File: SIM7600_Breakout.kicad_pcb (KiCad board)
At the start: 4 copper layers, 40 x 80 mm, 67 parts, among them J1 SIM8060-6-0-14-00-A, J2 2W Header, J3 MJ-3502N, J4 30W Header, J5 USB_B_Micro, J6 U.FL-R-SMT-1(01), J7 U.FL-R-SMT-1(01), J8 U.FL-R-SMT-1(01), Q1 MMBT3904L_RFG, U1 NVT2008PW_118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

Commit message: Added USB C to schematic & half assed putting it on the PCB
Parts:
- added R24: 5K1, Resistor_SMD:R_0201_0603Metric_Pad0.64x0.40mm_HandSolder, F.Cu at (141.6, 67.8)
- added R5: 5K1, Resistor_SMD:R_0201_0603Metric_Pad0.64x0.40mm_HandSolder, F.Cu at (129.8, 67.8)
- J5: value USB_B_Micro -> 2137160001; footprint sim7600_breakout:USB3100-30-A -> sim7600_breakout:2137160001-USB-C
- moved J5 3.58 mm to (138.7, 70.5)
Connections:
- D3 pad C: /D- -> /D+
- D4 pad C: /D+ -> /D-
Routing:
- net /PWRKEY: track 39.0 -> 15.6 mm, vias 2 -> 0
- net unconnected-(J5-Pad6): track 11.8 -> 0.00 mm
- net /D-: track 21.3 -> 19.9 mm
- net GND: track 96.2 -> 95.0 mm, vias 83 -> 81
- net /D+: track 21.2 -> 20.1 mm

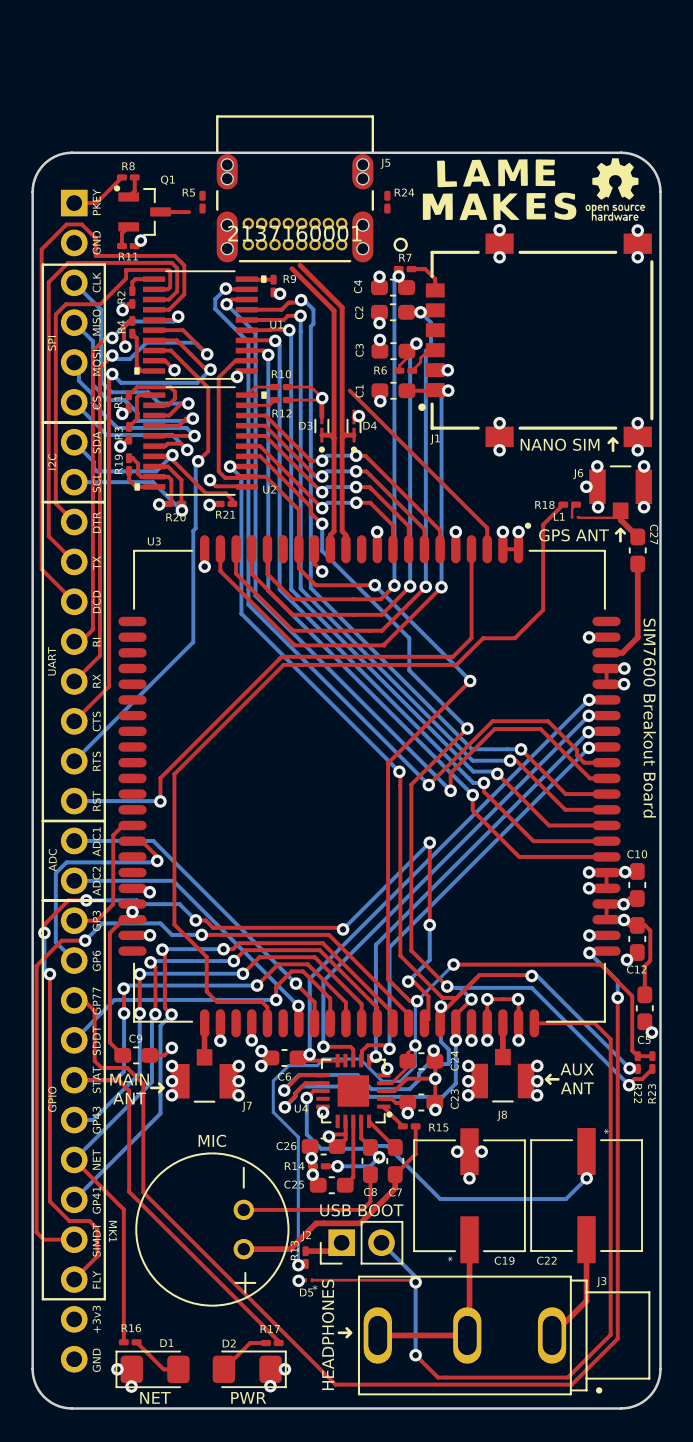
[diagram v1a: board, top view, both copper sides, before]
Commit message: Cleaning up USB-C addition
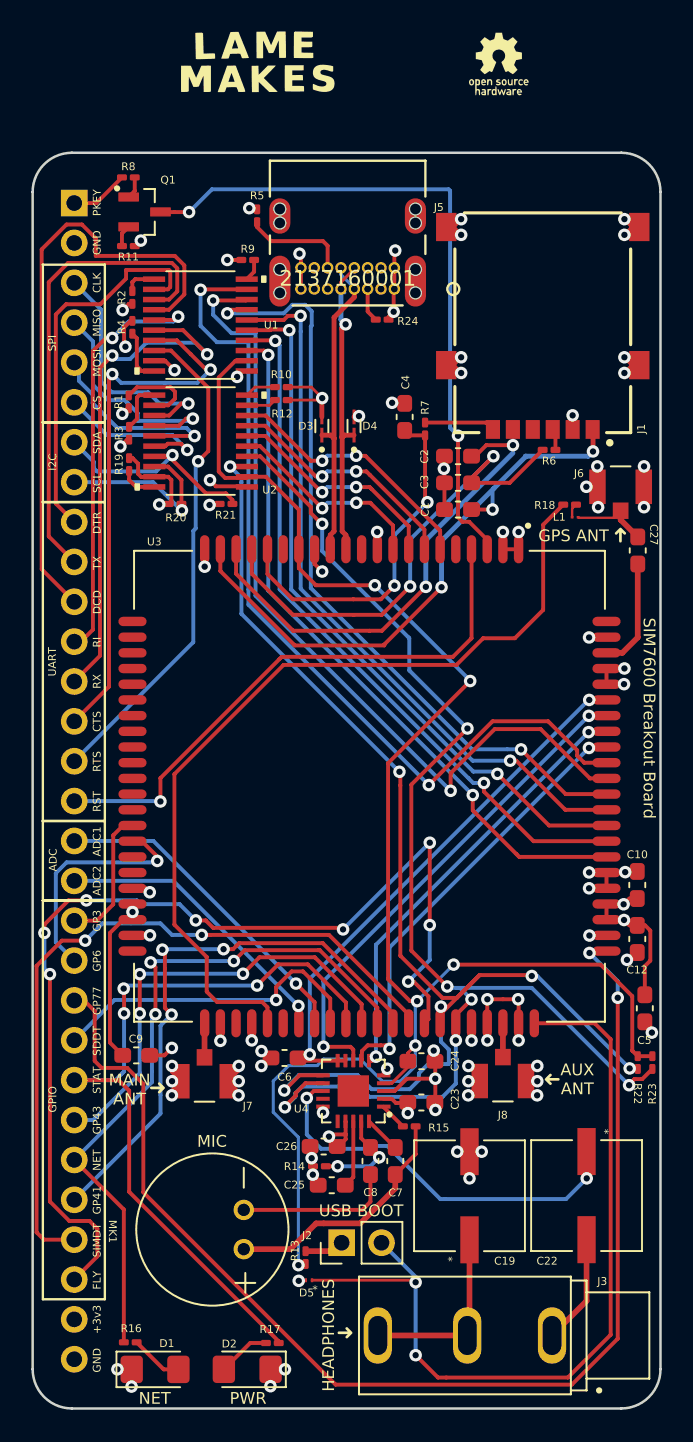
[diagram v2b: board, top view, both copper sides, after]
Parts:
- removed the G*** at (156.0, 83.3)
- moved G*** 17.4 mm to (133.3, 58.9)
- moved G*** 10.9 mm to (148.7, 59.0)
- moved R6 10.4 mm to (151.9, 83.6)
- moved R7 10.3 mm to (144.0, 82.3), turned to -90 degrees
- moved C2 10.1 mm to (146.1, 84.0)
- moved C3 9.35 mm to (146.1, 85.7)
- moved C1 8.61 mm to (146.1, 87.4)
- moved C4 8.27 mm to (142.7, 81.5), turned to 90 degrees
- moved R24 7.49 mm to (141.3, 75.3), turned to 180 degrees
- moved J5 4.38 mm to (142.0, 73.3)
- moved R5 3.58 mm to (133.3, 68.7), turned to -90 degrees
- moved R9 2.34 mm to (132.7, 71.5), turned to 0 degrees
- moved J1 1.12 mm to (151.5, 75.5), turned to 180 degrees
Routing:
- net /PWRKEY: track 15.6 -> 43.2 mm, vias 0 -> 2
- net /SIM_DATA: track 31.9 -> 22.6 mm
- net GND: track 95.0 -> 104.2 mm, vias 81 -> 82
- net Net-(J5-CC2): track 0.00 -> 6.71 mm
- net /SIM_CLK: track 36.1 -> 30.6 mm
- net /SIM_VCC: track 34.4 -> 38.1 mm, vias 2 -> 3
- net /UART_DTR: track 53.2 -> 56.0 mm
- net /UART_TX: track 51.8 -> 54.1 mm
- net /UART_DCD: track 46.8 -> 49.0 mm
- net Net-(J5-CC1): track 0.00 -> 2.16 mm
- net Net-(J1-IO): track 2.50 -> 4.51 mm
- net Net-(J1-RST): track 2.17 -> 1.37 mm
- net /D+: track 20.1 -> 19.8 mm, vias 0 -> 1
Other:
- board text removed: "NANO SIM"

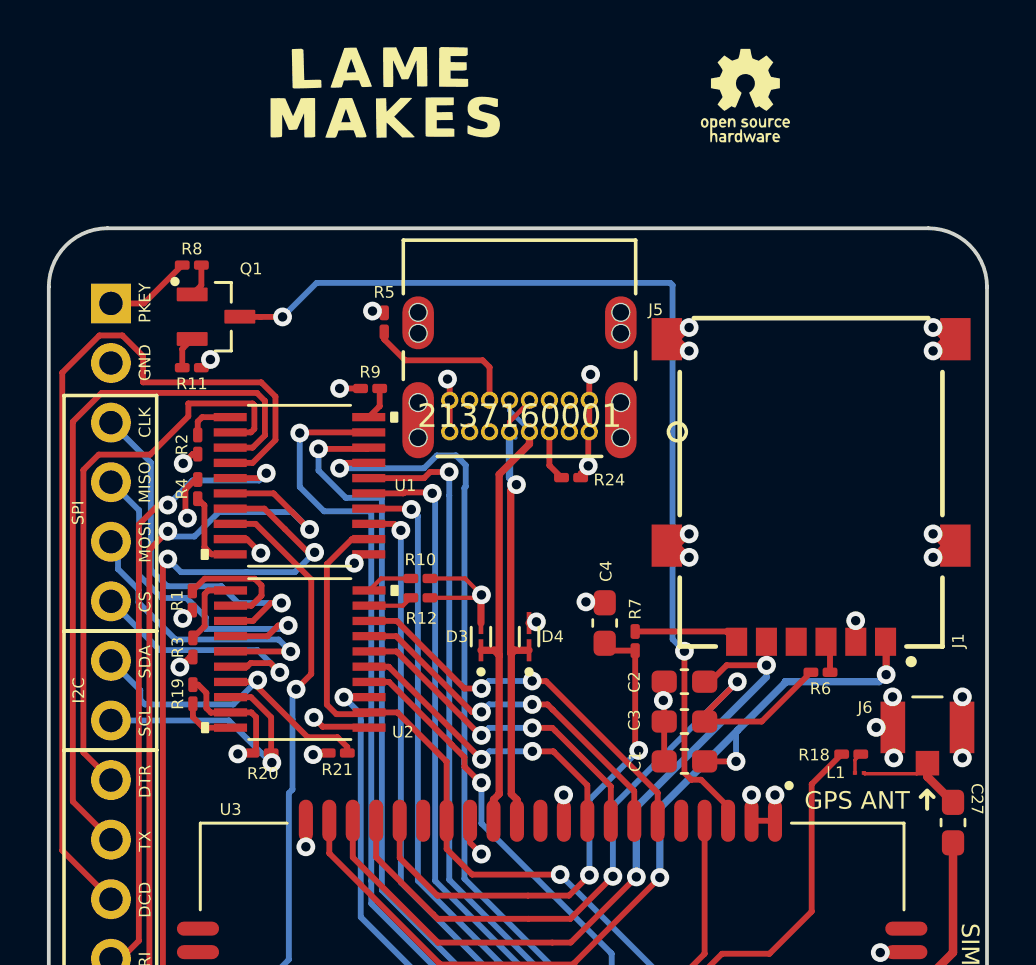
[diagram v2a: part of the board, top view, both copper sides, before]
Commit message: "it's USB 2.0 I don't care", logo updates
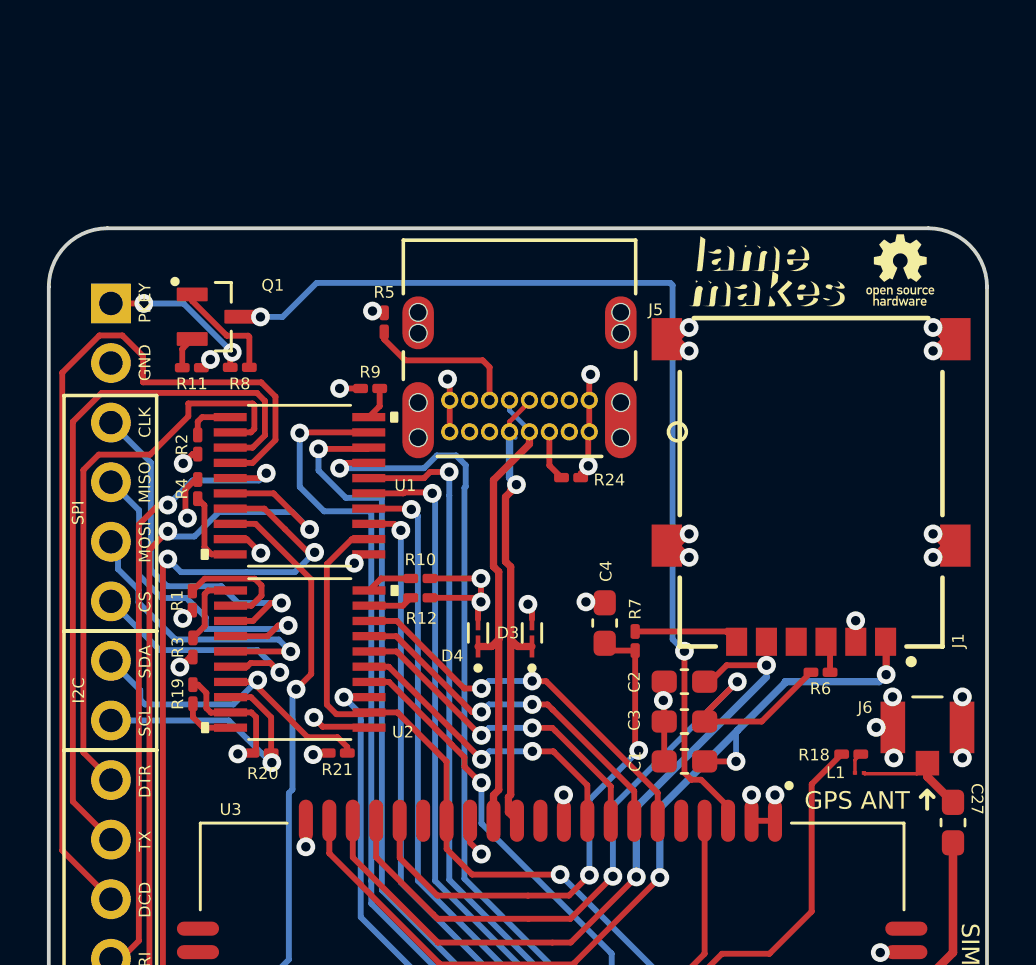
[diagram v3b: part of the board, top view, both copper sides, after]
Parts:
- moved G*** 18.0 mm to (149.6, 66.5)
- moved G*** 9.95 mm to (155.3, 66.5)
- moved R8 4.82 mm to (127.1, 70.6)
- moved D3 2.18 mm to (139.6, 81.9)
- moved D4 2.18 mm to (137.3, 81.9)
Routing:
- net Net-(Q1-Pad1): track 1.41 -> 4.65 mm
- net /PWR_ON: track 3.72 -> 6.71 mm, vias 0 -> 2
- net GND: track 104.2 -> 104.9 mm, vias 82 -> 83
